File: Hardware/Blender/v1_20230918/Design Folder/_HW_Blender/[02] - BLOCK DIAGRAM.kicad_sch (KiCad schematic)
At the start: 0 parts

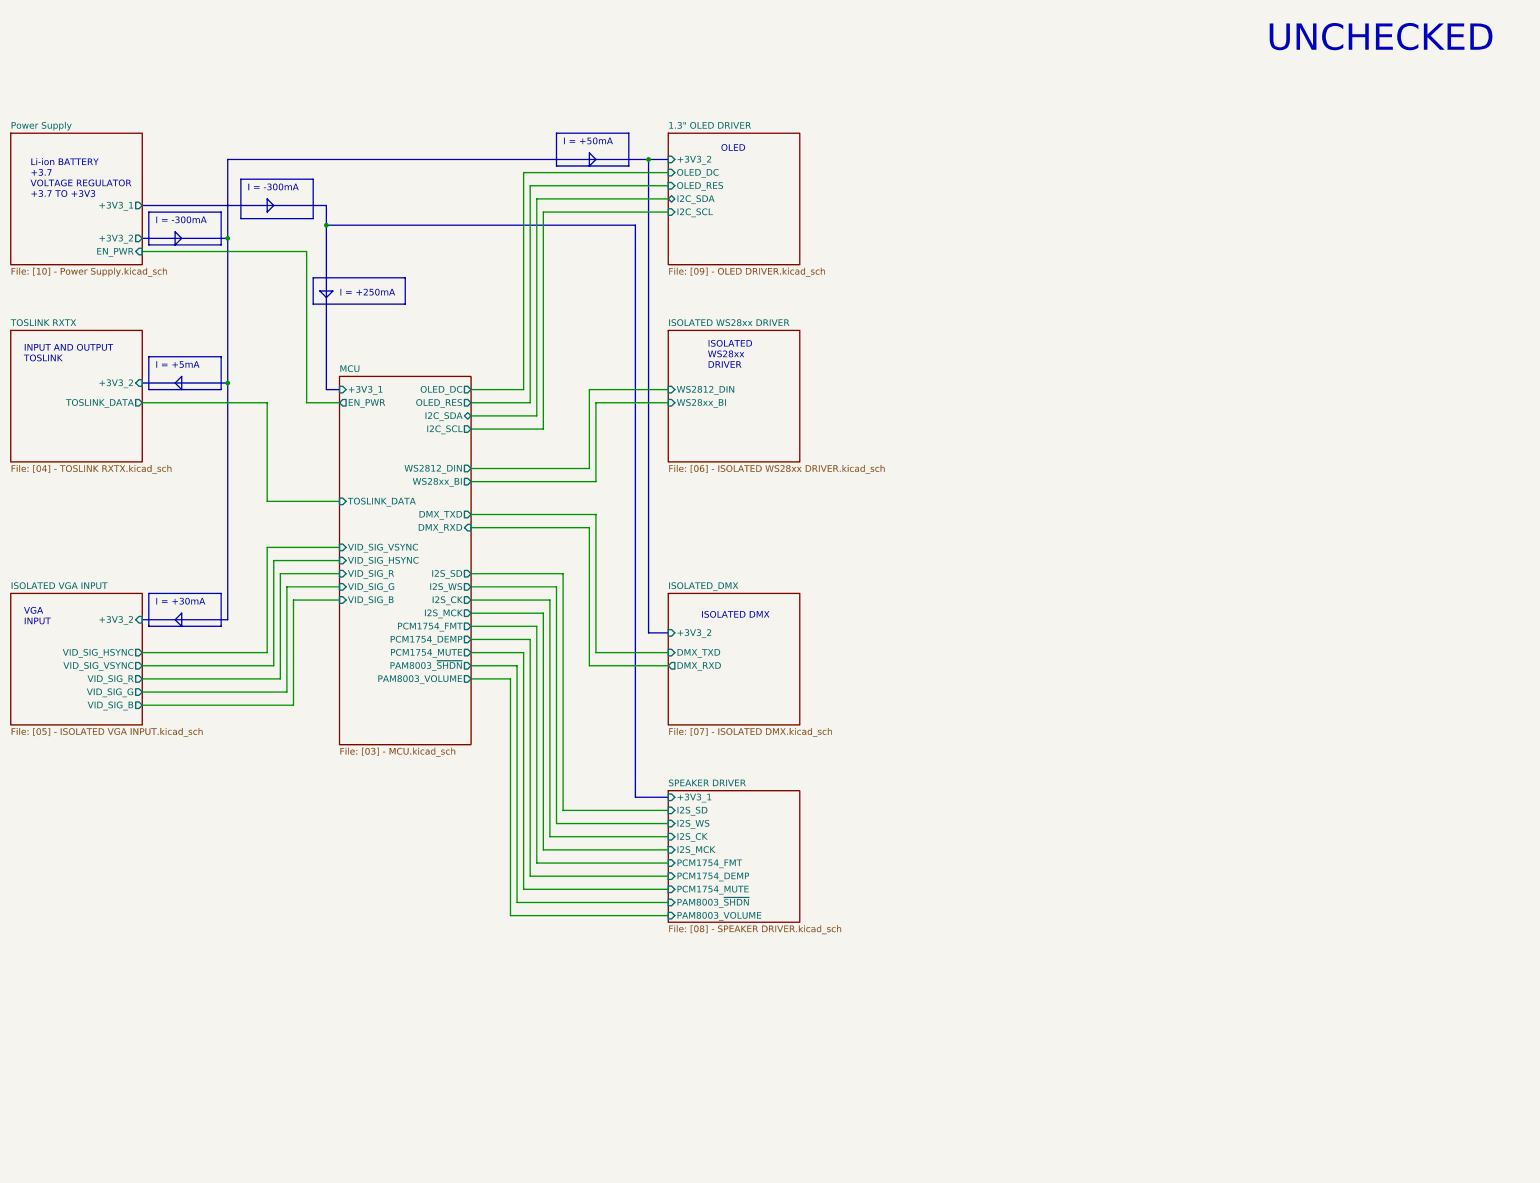
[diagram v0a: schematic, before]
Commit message: Improving the file structure and documentation
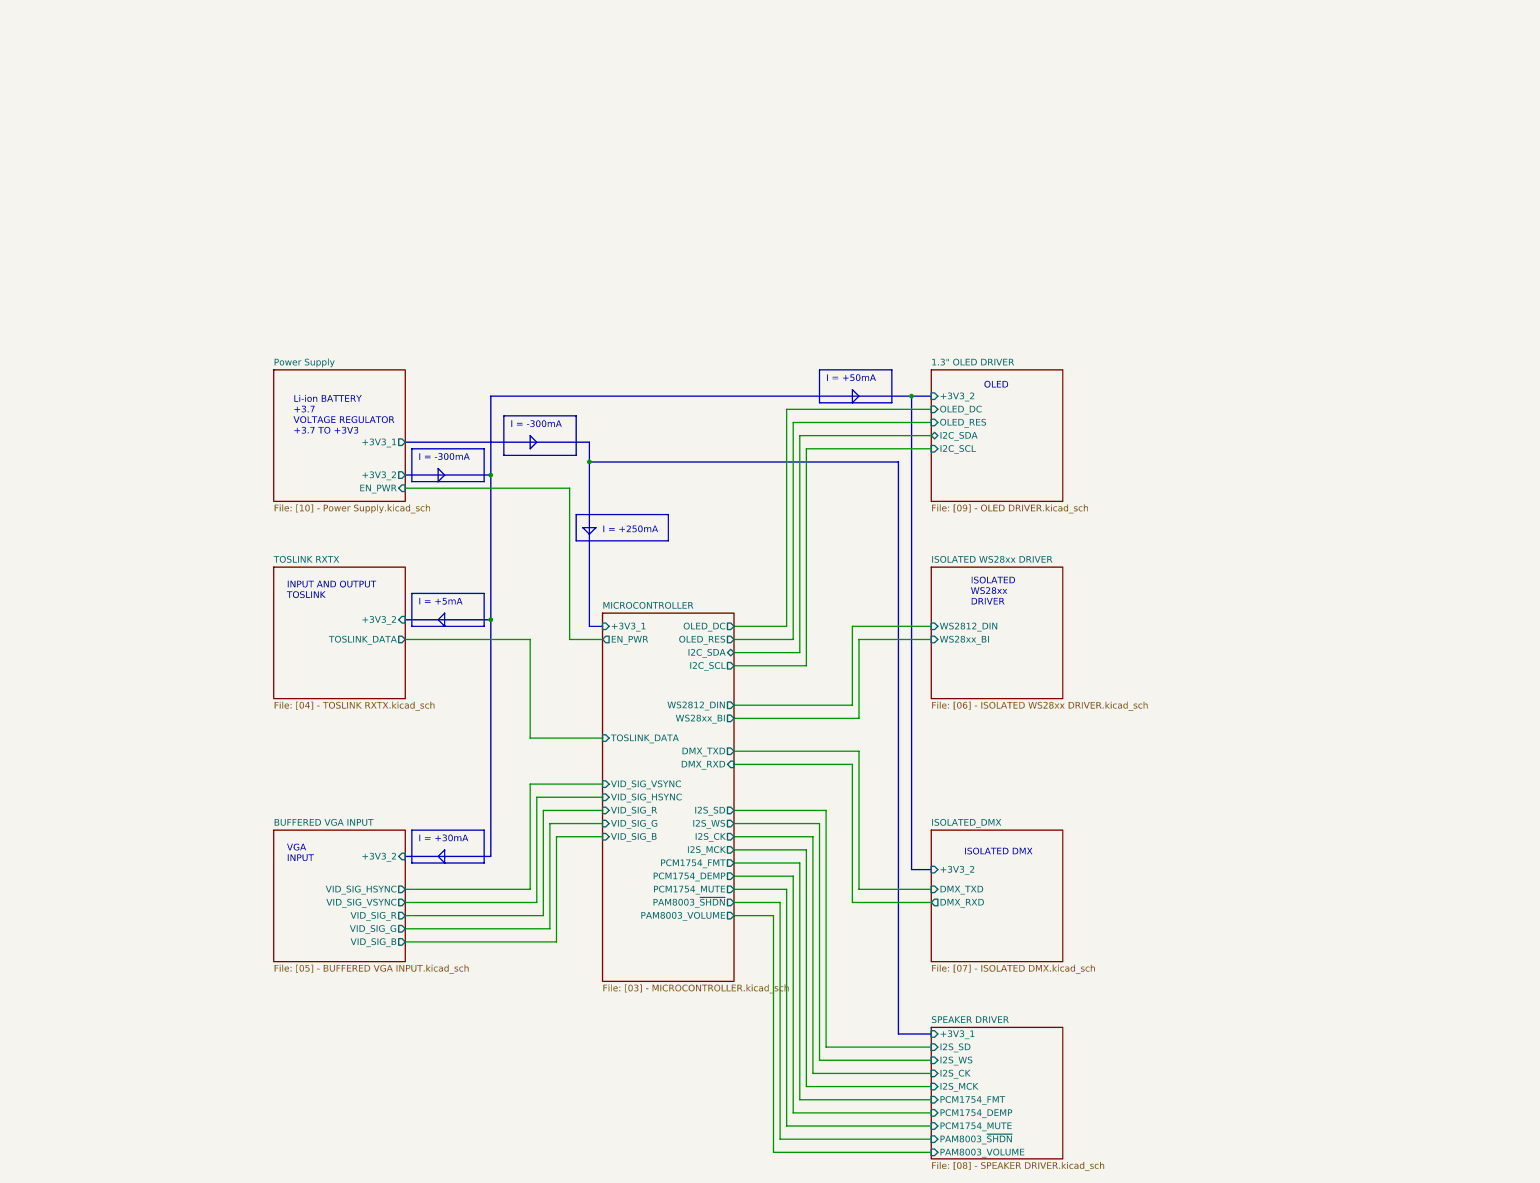
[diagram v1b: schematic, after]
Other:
- sheet ISOLATED VGA INPUT renamed BUFFERED VGA INPUT
- sheet MCU renamed MICROCONTROLLER
- sheet BUFFERED VGA INPUT: file [05] - ISOLATED VGA INPUT.kicad_sch -> [05] - BUFFERED VGA INPUT.kicad_sch
- sheet MICROCONTROLLER: file [03] - MCU.kicad_sch -> [03] - MICROCONTROLLER.kicad_sch
- note removed: "UNCHECKED"
